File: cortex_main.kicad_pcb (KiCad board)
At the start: 2 copper layers, 141 x 129.5 mm, 35 parts, among them J1 TEST_1P, J2 TEST_1P, P1 CONN_01X04, P10 CONN_01X03, P11 CONN_01X03, P12 CONN_01X03, P13 CONN_01X03, P14 CONN_01X03, P15 CONN_01X03, P16 CONN_01X02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

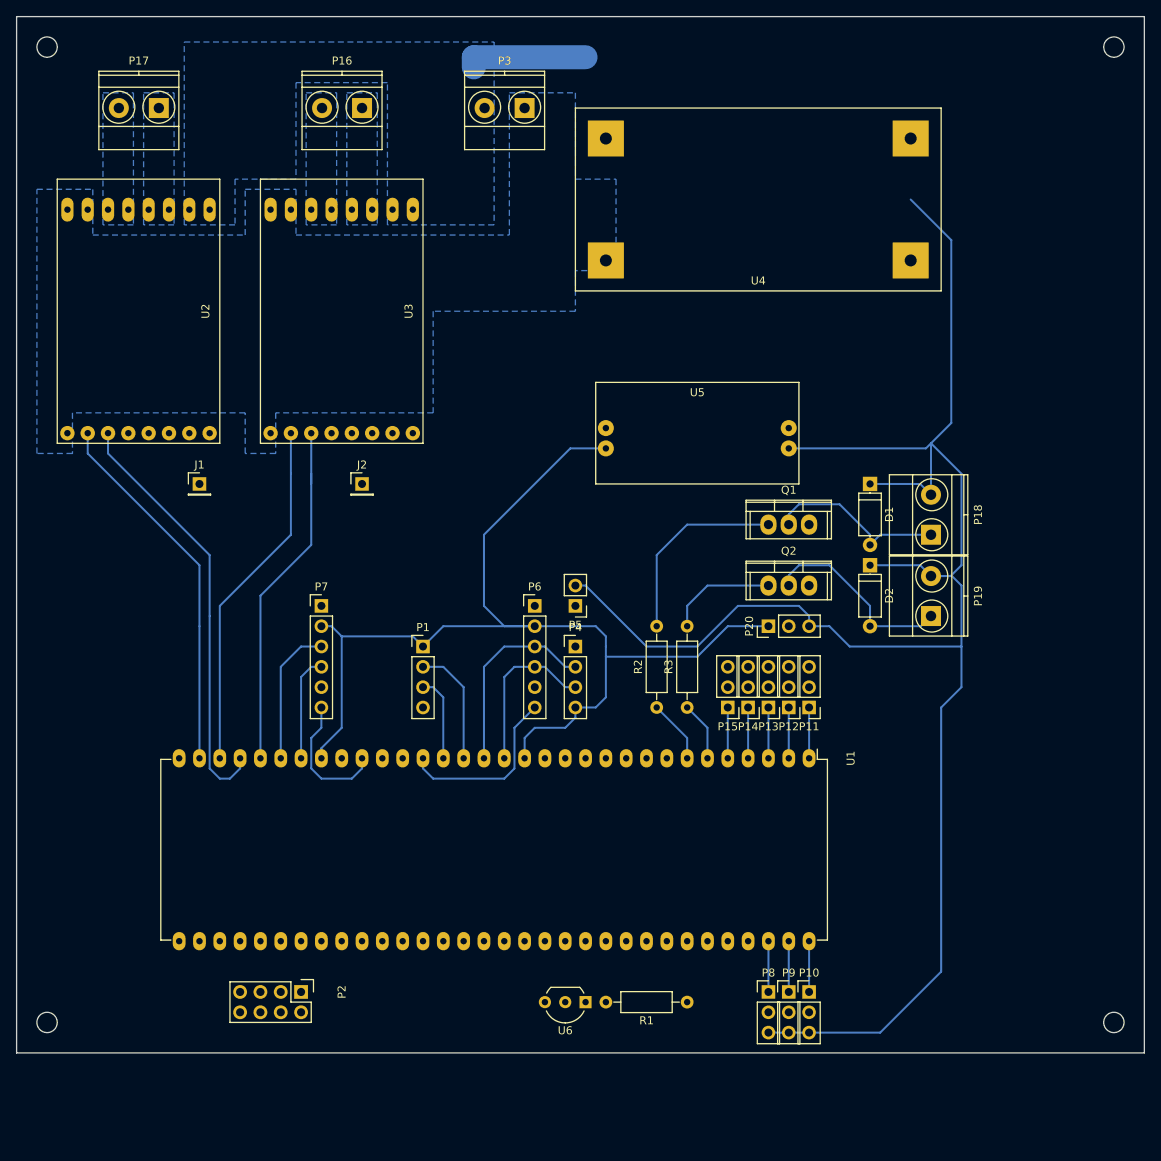
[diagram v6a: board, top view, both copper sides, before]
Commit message: cortex: add vacuum pump mosfets
on both schematic & layout.

Signed-off-by: Yannick Gicquel <ygicquel@gmail.com>
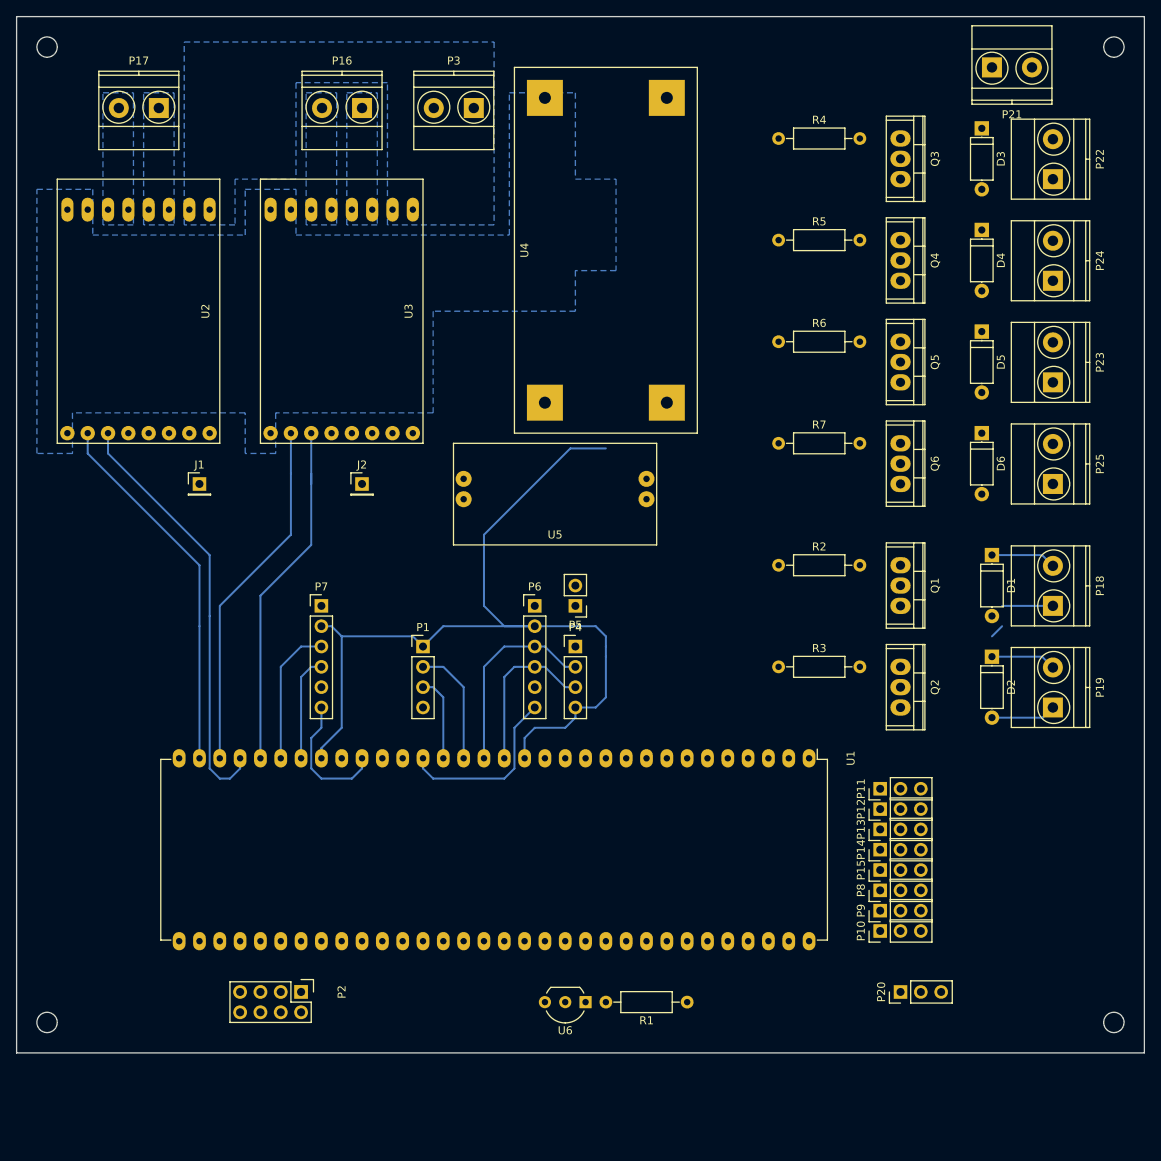
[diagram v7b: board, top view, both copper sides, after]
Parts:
- added D3: 1N4001, Diodes_ThroughHole:D_A-405_P7.62mm_Horizontal, F.Cu at (153.7, 41.9)
- added D4: 1N4001, Diodes_ThroughHole:D_A-405_P7.62mm_Horizontal, F.Cu at (153.7, 54.6)
- added D5: 1N4001, Diodes_ThroughHole:D_A-405_P7.62mm_Horizontal, F.Cu at (153.7, 67.3)
- added D6: 1N4001, Diodes_ThroughHole:D_A-405_P7.62mm_Horizontal, F.Cu at (153.7, 80.0)
- added P21: CONN_01X02, Terminal_Blocks:TerminalBlock_Pheonix_MKDS1.5-2pol, F.Cu at (154.9, 34.3)
- added P22: CONN_01X02, Terminal_Blocks:TerminalBlock_Pheonix_MKDS1.5-2pol, F.Cu at (162.6, 48.3)
- added P23: CONN_01X02, Terminal_Blocks:TerminalBlock_Pheonix_MKDS1.5-2pol, F.Cu at (162.6, 73.7)
- added P24: CONN_01X02, Terminal_Blocks:TerminalBlock_Pheonix_MKDS1.5-2pol, F.Cu at (162.6, 61.0)
- added P25: CONN_01X02, Terminal_Blocks:TerminalBlock_Pheonix_MKDS1.5-2pol, F.Cu at (162.6, 86.4)
- added Q3: IRF540N, Power_Integrations:TO-220, F.Cu at (143.5, 45.7)
- added Q4: IRF540N, Power_Integrations:TO-220, F.Cu at (143.5, 58.4)
- added Q5: IRF540N, Power_Integrations:TO-220, F.Cu at (143.5, 71.1)
- added Q6: IRF540N, Power_Integrations:TO-220, F.Cu at (143.5, 83.8)
- added R4: 100R, Resistors_ThroughHole:R_Axial_DIN0207_L6.3mm_D2.5mm_P10.16mm_Horizontal, F.Cu at (128.3, 43.2)
- added R5: 100R, Resistors_ThroughHole:R_Axial_DIN0207_L6.3mm_D2.5mm_P10.16mm_Horizontal, F.Cu at (128.3, 55.9)
- added R6: 100R, Resistors_ThroughHole:R_Axial_DIN0207_L6.3mm_D2.5mm_P10.16mm_Horizontal, F.Cu at (128.3, 68.6)
- added R7: 100R, Resistors_ThroughHole:R_Axial_DIN0207_L6.3mm_D2.5mm_P10.16mm_Horizontal, F.Cu at (128.3, 81.3)
- moved P20 48.6 mm to (143.5, 149.9)
- moved P15 27.9 mm to (141.0, 134.6), turned to 90 degrees
- moved P14 24.3 mm to (141.0, 132.1), turned to 90 degrees
- moved R2 23.4 mm to (128.3, 96.5), turned to 0 degrees
- moved P13 20.7 mm to (141.0, 129.5), turned to 90 degrees
- moved U4 20.1 mm to (106.7, 57.1), turned to 270 degrees
- moved U5 19.3 mm to (100.3, 87.6), turned to 0 degrees
- moved D2 19.1 mm to (154.9, 108.0)
- moved P19 19.1 mm to (162.6, 114.3)
- moved P8 18.9 mm to (141.0, 137.2), turned to 90 degrees
- moved Q2 18.9 mm to (143.5, 111.8), turned to 270 degrees
- moved D1 17.6 mm to (154.9, 95.2)
- moved P18 17.6 mm to (162.6, 101.6)
- moved P12 17.1 mm to (141.0, 127.0), turned to 90 degrees
- moved Q1 15.9 mm to (143.5, 99.1), turned to 270 degrees
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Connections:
- U1 pad 10: Net-(U1-Pad10) -> /Sheet_MCU/CMD_PUMP_TR
- U1 pad 11: Net-(U1-Pad11) -> /Sheet_MCU/CMD_PUMP_TL
- U1 pad 8: Net-(U1-Pad8) -> /Sheet_MCU/CMD_PUMP_BR
- U1 pad 9: Net-(U1-Pad9) -> /Sheet_MCU/CMD_PUMP_BL
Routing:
- net OUTP_ARMMOTOR_L: track 216.4 -> 16.4 mm
- net Net-(Q1-Pad1): track 24.4 -> 0.00 mm
- net +3V3: track 135.6 -> 113.7 mm
- net OUTN_ARMMOTOR_R: track 24.7 -> 8.15 mm
- net OUTN_ARMMOTOR_L: track 23.0 -> 6.35 mm
- net IR_VCC: track 14.0 -> 0.00 mm
- net Net-(Q2-Pad1): track 13.8 -> 0.00 mm
- net (no net): track 15.2 -> 1.80 mm
- net /Sheet_MCU/CMD_ARMMOTOR_L: track 7.93 -> 0.00 mm
- net /Sheet_MCU/CMD_ARMMOTOR_R: track 7.40 -> 0.00 mm
- net IR_VIN_2: track 6.35 -> 0.00 mm
- net IR_VIN_1: track 6.35 -> 0.00 mm
- net IR_VIN_0: track 6.35 -> 0.00 mm
- net IR_VIN_7: track 6.35 -> 0.00 mm
- net IR_VIN_6: track 6.35 -> 0.00 mm
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
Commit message: cortex: update arm motors PSU
PCB is almost done.

Signed-off-by: Yannick Gicquel <ygicquel@gmail.com>
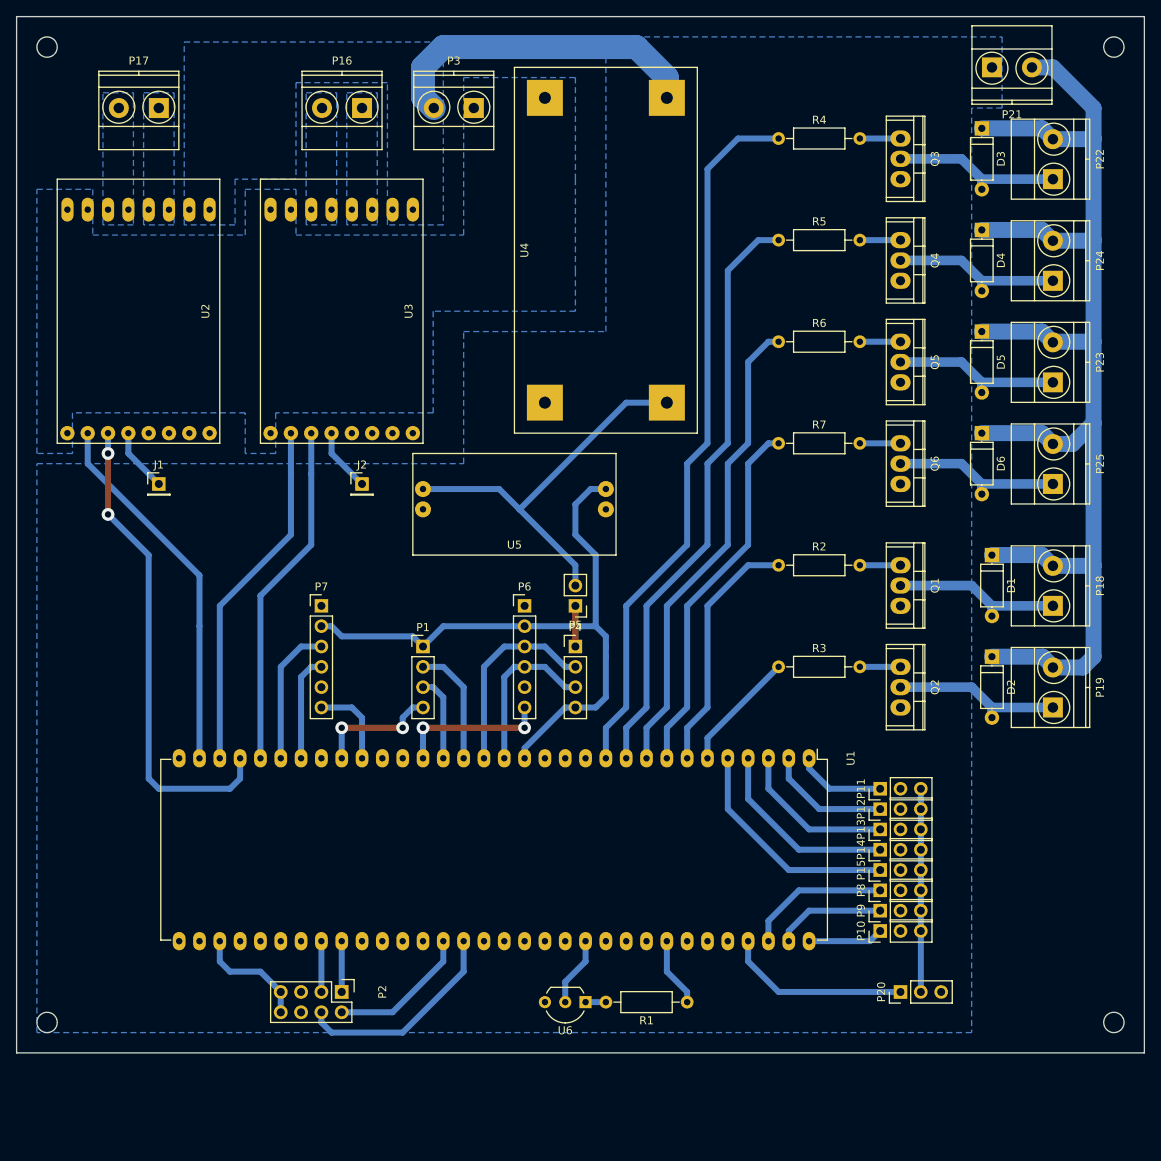
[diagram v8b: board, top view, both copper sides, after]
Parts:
- moved U5 5.24 mm to (95.2, 88.9)
- moved J1 5.08 mm to (50.8, 86.4)
- moved P2 5.08 mm to (73.7, 149.9)
- moved P6 1.27 mm to (96.5, 101.6)
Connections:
- D3 pad 1: OUTP_PUMP_BL -> OUTP_ARMMOTOR_L
- D4 pad 1: OUTP_PUMP_BL -> OUTP_ARMMOTOR_L
- D5 pad 1: OUTP_PUMP_BL -> OUTP_ARMMOTOR_L
- D6 pad 1: OUTP_PUMP_BL -> OUTP_ARMMOTOR_L
- P20 pad 3: OUTP_ARMMOTOR_L -> +5V
- P21 pad 2: OUTP_PUMP_BL -> OUTP_ARMMOTOR_L
- P22 pad 2: OUTP_PUMP_BL -> OUTP_ARMMOTOR_L
- P23 pad 2: OUTP_PUMP_BL -> OUTP_ARMMOTOR_L
- P24 pad 2: OUTP_PUMP_BL -> OUTP_ARMMOTOR_L
- P25 pad 2: OUTP_PUMP_BL -> OUTP_ARMMOTOR_L
- P5 pad 2: OUTP_ARMMOTOR_L -> +5V
- U1 pad 46: ENCA_R -> ENCB_R
- U1 pad 47: ENCB_R -> ENCA_R
- U4 pad 3: OUTP_ARMMOTOR_L -> +5V
- U5 pad 1: OUTP_ARMMOTOR_L -> +5V
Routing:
- net OUTP_ARMMOTOR_L: track 16.4 -> 164.9 mm
- net /Sheet_MCU/CMD_PUMP_TL: track 0.00 -> 89.4 mm
- net /Sheet_MCU/CMD_PUMP_TR: track 0.00 -> 74.1 mm
- net /Sheet_MCU/CMD_PUMP_BL: track 0.00 -> 59.7 mm
- net +5V: track 0.00 -> 49.5 mm
- net /Sheet_MCU/CMD_PUMP_BR: track 0.00 -> 45.9 mm
- net +24V: track 0.00 -> 41.3 mm
- net /Sheet_MCU/CMD_ARMMOTOR_L: track 0.00 -> 31.1 mm
- net IR_VIN_7: track 0.00 -> 28.6 mm
- net ENCA_R: track 0.00 -> 26.5 mm
- net IR_VCC: track 0.00 -> 25.4 mm
- net IR_VIN_6: track 0.00 -> 24.2 mm
- net OUTN_PUMP_TL: track 0.00 -> 21.4 mm
- net OUTN_PUMP_BL: track 0.00 -> 21.4 mm
- net OUTN_PUMP_BR: track 0.00 -> 21.4 mm
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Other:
- net class Default: trace_width 0.25 -> 0.75; via_dia 0.6 -> 1.6; via_drill 0.4 -> 0.8
- net class MedPower2mm added: clearance 0.2, trace_width 2, via_dia 1.6, via_drill 0.8
- net class Power added: clearance 0.2, trace_width 1.2, via_dia 1.6, via_drill 0.8
